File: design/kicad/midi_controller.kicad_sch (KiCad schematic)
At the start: 4 parts, among them U1 CD74HC4067M

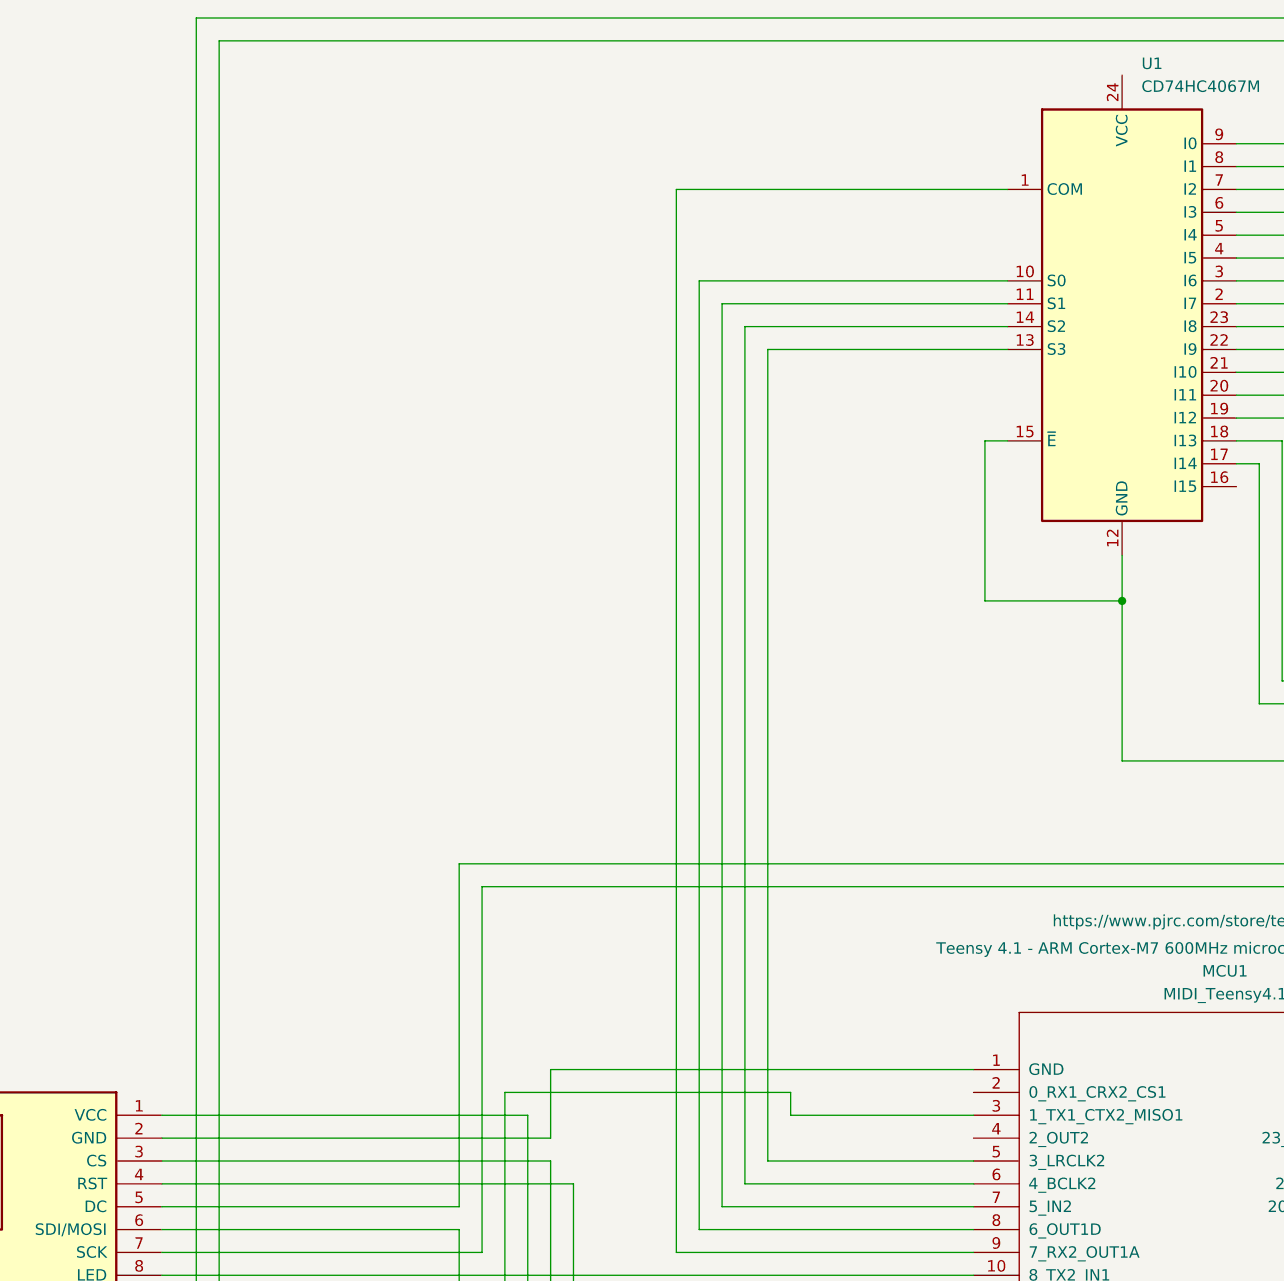
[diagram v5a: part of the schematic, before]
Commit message: Update kicad binary files - update 3d models
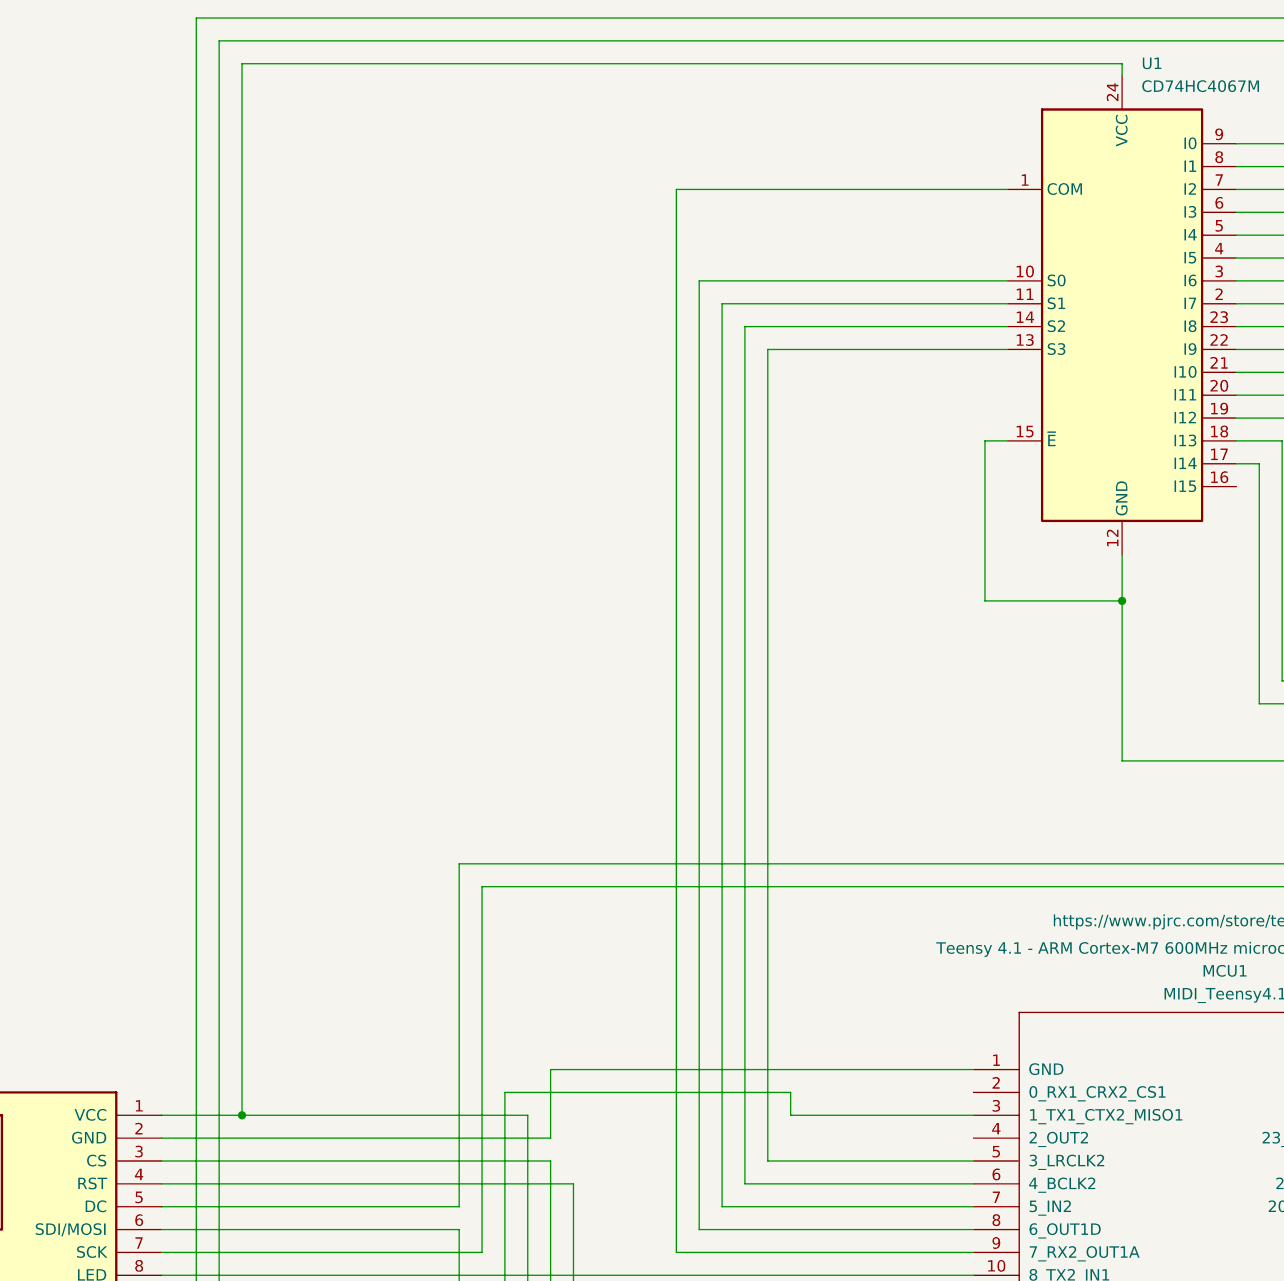
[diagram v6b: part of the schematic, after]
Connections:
- net at D1.1 (VCC), MCU1.15 (3V3): now also U1.24 (VCC)
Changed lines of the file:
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@@
+	)
+	(junction
+		(at 77.47 182.88)
+		(diameter 0)
+		(color 0 0 0 0)
 	)
 	(junction
@@
 	(wire
 		(pts
-			(xy 68.58 182.88) (xy 109.22 182.88)
+			(xy 68.58 182.88) (xy 77.47 182.88)
+		)
+		(stroke
+			(width 0)
+			(type default)
+		)
+	)
+	(wire
+		(pts
+			(xy 175.26 66.04) (xy 77.47 66.04)
 		)
 		(stroke
@@
 		)
 	)
+	(wire
+		(pts
+			(xy 77.47 182.88) (xy 109.22 182.88)
+		)
+		(stroke
+			(width 0)
+			(type default)
+		)
+	)
 	(bus
 		(pts
@@
 	(wire
 		(pts
+			(xy 175.26 67.31) (xy 175.26 66.04)
+		)
+		(stroke
+			(width 0)
+			(type default)
+		)
+	)
+	(wire
+		(pts
 			(xy 214.63 233.68) (xy 295.91 233.68)
 		)
@@
 		)
 		(stroke
+			(width 0)
+			(type default)
+		)
+	)
+	(wire
+		(pts
+			(xy 77.47 66.04) (xy 77.47 182.88)
+		)
+		(stroke

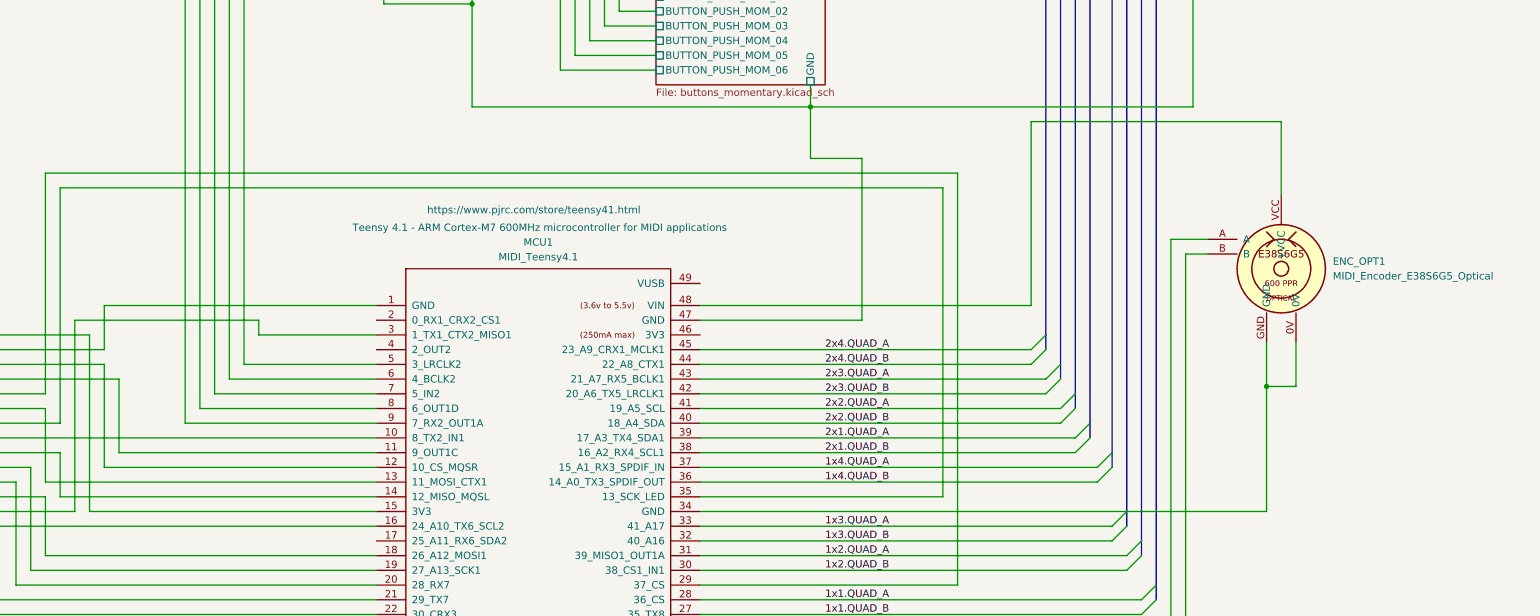
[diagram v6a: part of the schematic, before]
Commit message: Update kicad binary files
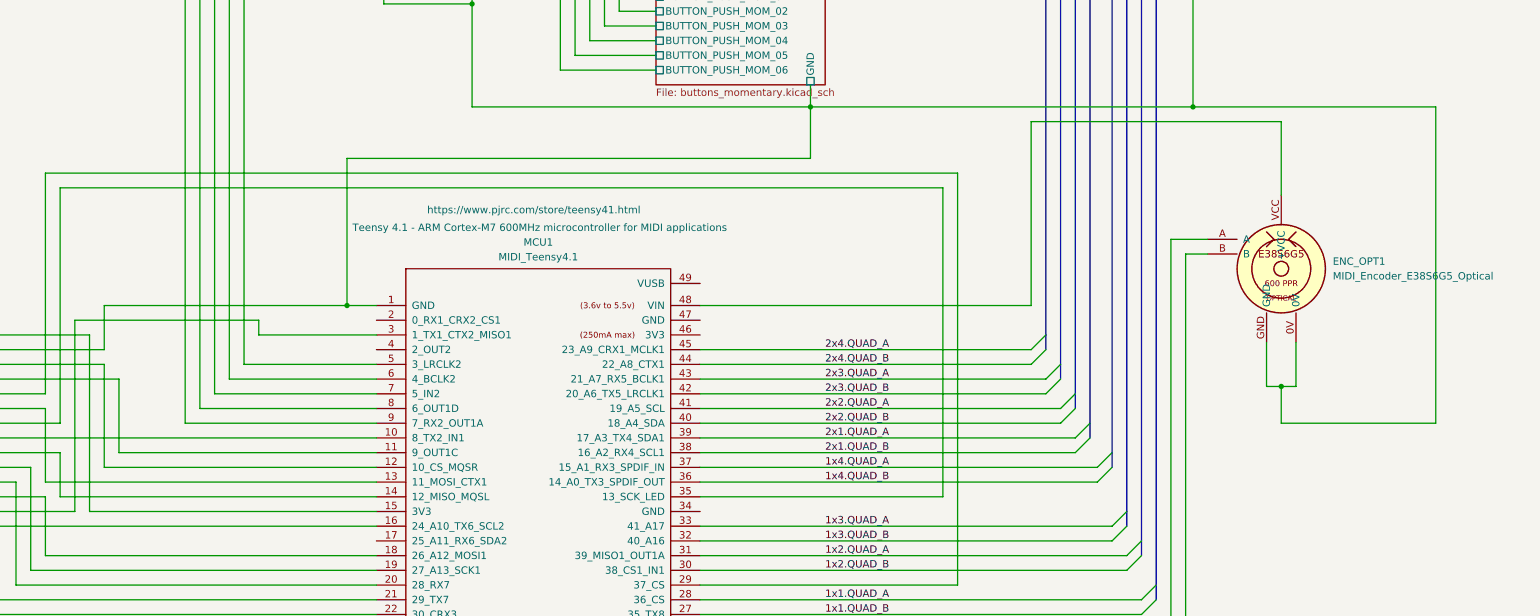
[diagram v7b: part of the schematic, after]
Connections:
- net Buttons_Momentary/GND: now also D1.2 (GND), ENC_OPT1.0V, ENC_OPT1.GND, MCU1.1 (GND); no longer MCU1.47 (GND)
- now unconnected: MCU1.34 (GND)
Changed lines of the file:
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@@
+	)
+	(junction
+		(at 299.72 143.51)
+		(diameter 0)
+		(color 0 0 0 0)
 	)
 	(junction
@@
 	)
 	(junction
-		(at 312.42 191.77)
+		(at 314.96 191.77)
 		(diameter 0)
 		(color 0 0 0 0)
@@
 		(color 0 0 0 0)
 	)
+	(junction
+		(at 153.67 177.8)
+		(diameter 0)
+		(color 0 0 0 0)
+	)
 	(bus_entry
 		(at 290.83 218.44)
@@
 		)
 	)
-	(wire
-		(pts
-			(xy 214.63 213.36) (xy 288.29 213.36)
-		)
-		(stroke
-			(width 0)
-			(type default)
-		)
-	)
 	(bus
 		(pts
@@
 	(wire
 		(pts
-			(xy 242.57 180.34) (xy 242.57 152.4)
-		)
-		(stroke
-			(width 0)
-			(type default)
-		)
-	)
-	(wire
-		(pts
 			(xy 214.63 198.12) (xy 276.86 198.12)
 		)
@@
 	(wire
 		(pts
+			(xy 314.96 191.77) (xy 314.96 198.12)
+		)
+		(stroke
+			(width 0)
+			(type default)
+		)
+	)
+	(wire
+		(pts
 			(xy 213.36 105.41) (xy 213.36 63.5)
 		)
@@
 	(wire
 		(pts
-			(xy 312.42 191.77) (xy 317.5 191.77)
+			(xy 312.42 191.77) (xy 314.96 191.77)
 		)
 		(stroke
@@
 	(wire
 		(pts
+			(xy 341.63 143.51) (xy 299.72 143.51)
+		)
+		(stroke
+			(width 0)
+			(type default)
+		)
+	)
+	(wire
+		(pts
 			(xy 214.63 190.5) (xy 274.32 190.5)
 		)
@@
 	(wire
 		(pts
-			(xy 312.42 191.77) (xy 312.42 213.36)
-		)
-		(stroke
-			(width 0)
-			(type default)
-		)
-	)
-	(wire
-		(pts
 			(xy 175.26 120.65) (xy 175.26 125.73)
 		)
@@
 	(wire
 		(pts
+			(xy 341.63 198.12) (xy 341.63 143.51)
+		)
+		(stroke
+			(width 0)
+			(type default)
+		)
+	)
+	(wire
+		(pts
 			(xy 207.01 134.62) (xy 193.04 134.62)
 		)
@@
 	(wire
 		(pts
+			(xy 153.67 177.8) (xy 153.67 152.4)
+		)
+		(stroke
+			(width 0)
+			(type default)
+		)
+	)
+	(wire
+		(pts
 			(xy 187.96 77.47) (xy 260.35 77.47)
 		)
@@
 	(wire
 		(pts
-			(xy 242.57 152.4) (xy 233.68 152.4)
-		)
-		(stroke
-			(width 0)
-			(type default)
-		)
-	)
-	(wire
-		(pts
 			(xy 101.6 154.94) (xy 259.08 154.94)
 		)
@@
 	(wire
 		(pts
+			(xy 153.67 177.8) (xy 158.75 177.8)
+		)
+		(stroke
+			(width 0)
+			(type default)
+		)
+	)
+	(wire
+		(pts
 			(xy 214.63 187.96) (xy 271.78 187.96)
 		)
@@
 	(wire
 		(pts
+			(xy 153.67 152.4) (xy 233.68 152.4)
+		)
+		(stroke
+			(width 0)
+			(type default)
+		)
+	)
+	(wire
+		(pts
 			(xy 214.63 210.82) (xy 256.54 210.82)
 		)
@@
 	(wire
 		(pts
+			(xy 314.96 198.12) (xy 341.63 198.12)
+		)
+		(stroke
+			(width 0)
+			(type default)
+		)
+	)
+	(wire
+		(pts
 			(xy 135.89 97.79) (xy 162.56 97.79)
 		)
@@
 	(wire
 		(pts
-			(xy 111.76 177.8) (xy 158.75 177.8)
+			(xy 111.76 177.8) (xy 153.67 177.8)
 		)
 		(stroke
@@
 		)
 	)
-	(wire
-		(pts
-			(xy 214.63 180.34) (xy 242.57 180.34)
-		)
-		(stroke
-			(width 0)
-			(type default)
-		)
-	)
 	(bus
 		(pts
@@
 	(wire
 		(pts
+			(xy 314.96 191.77) (xy 317.5 191.77)
+		)
+		(stroke
+			(width 0)
+			(type default)
+		)
+	)
+	(wire
+		(pts
 			(xy 295.91 166.37) (xy 295.91 233.68)
 		)
 		(stroke
-			(width 0)
-			(type default)
-		)
-	)
-	(wire
-		(pts
-			(xy 312.42 213.36) (xy 288.29 213.36)
-		)
-		(stroke
